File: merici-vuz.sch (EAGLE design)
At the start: 51 parts, among them IC1 MEGA328-PB, IC2 MCP73831, IC3 LE33, Q1 3,6864 MHz, Q2 IRLML6402PBF, Q4 TSM2302CX

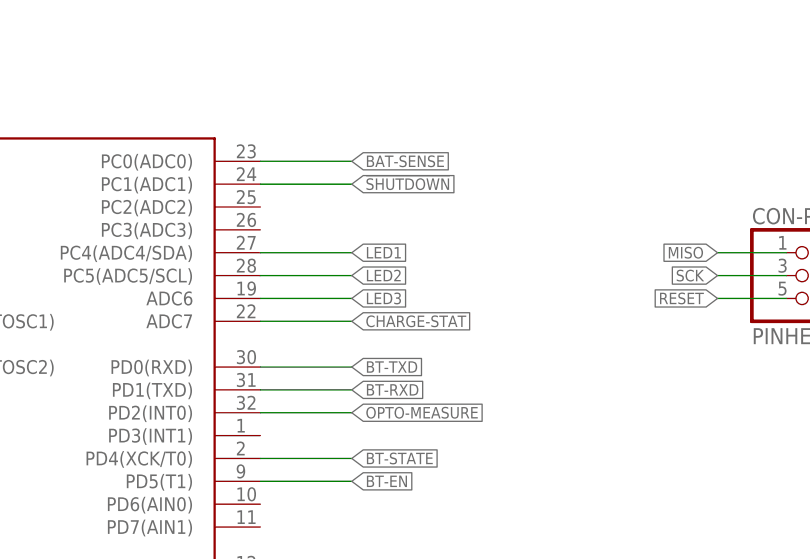
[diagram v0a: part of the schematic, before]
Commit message: Fix unconnected LEDS.
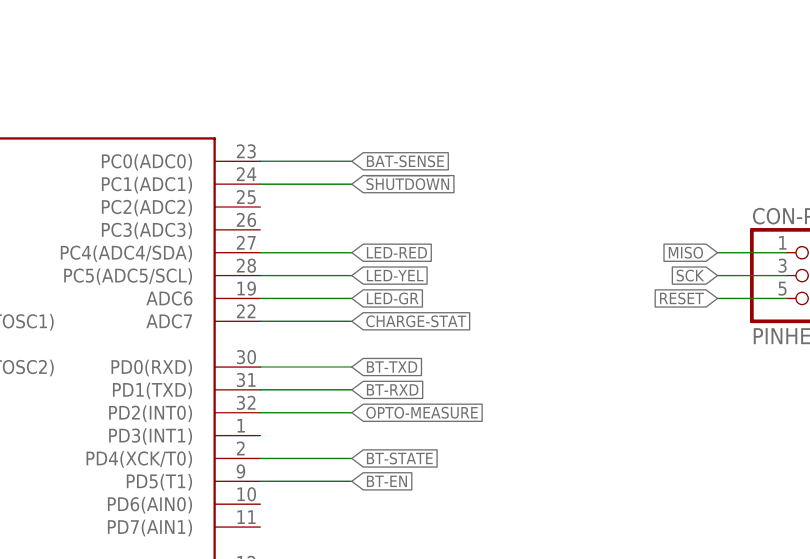
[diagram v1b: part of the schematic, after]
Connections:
- removed net LED1: IC1.PC4(ADC4/SDA)
- removed net LED2: IC1.PC5(ADC5/SCL)
- removed net LED3: IC1.ADC6
- net LED-GR: now also IC1.ADC6
- net LED-RED: now also IC1.PC4(ADC4/SDA)
- net LED-YEL: now also IC1.PC5(ADC5/SCL)
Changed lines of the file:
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@@
-</segment>
-</net>
-<net name="LED1" class="0">
-<segment>
-<pinref part="IC1" gate="G$1" pin="PC4(ADC4/SDA)"/>
-<wire x1="91.44" y1="147.32" x2="101.6" y2="147.32" width="0.1524" layer="91"/>
-<label x="101.6" y="147.32" size="1.27" layer="95" xref="yes"/>
-</segment>
-</net>
-<net name="LED2" class="0">
-<segment>
-<pinref part="IC1" gate="G$1" pin="PC5(ADC5/SCL)"/>
-<wire x1="91.44" y1="144.78" x2="101.6" y2="144.78" width="0.1524" layer="91"/>
-<label x="101.6" y="144.78" size="1.27" layer="95" xref="yes"/>
-</segment>
-</net>
-<net name="LED3" class="0">
-<segment>
-<pinref part="IC1" gate="G$1" pin="ADC6"/>
-<wire x1="91.44" y1="142.24" x2="101.6" y2="142.24" width="0.1524" layer="91"/>
-<label x="101.6" y="142.24" size="1.27" layer="95" xref="yes"/>
 </segment>
 </net>
@@
 <label x="223.52" y="129.54" size="1.27" layer="95" rot="R270" xref="yes"/>
 </segment>
+<segment>
+<pinref part="IC1" gate="G$1" pin="PC4(ADC4/SDA)"/>
+<wire x1="91.44" y1="147.32" x2="101.6" y2="147.32" width="0.1524" layer="91"/>
+<label x="101.6" y="147.32" size="1.27" layer="95" xref="yes"/>
+</segment>
 </net>
 <net name="LED-YEL" class="0">
@@
 <label x="233.68" y="129.54" size="1.27" layer="95" rot="R270" xref="yes"/>
 </segment>
+<segment>
+<pinref part="IC1" gate="G$1" pin="PC5(ADC5/SCL)"/>
+<wire x1="91.44" y1="144.78" x2="101.6" y2="144.78" width="0.1524" layer="91"/>
+<label x="101.6" y="144.78" size="1.27" layer="95" xref="yes"/>
+</segment>
 </net>
 <net name="LED-GR" class="0">
@@
 <label x="243.84" y="129.54" size="1.27" layer="95" rot="R270" xref="yes"/>
 </segment>
-</net>
+<segment>
+<pinref part="IC1" gate="G$1" pin="ADC6"/>
+<wire x1="91.44" y1="142.24" x2="101.6" y2="142.24" width="0.1524" layer="91"/>
+<label x="101.6" y="142.24" size="1.27" layer="95" xref="yes"/>
+</segment>
+</net>

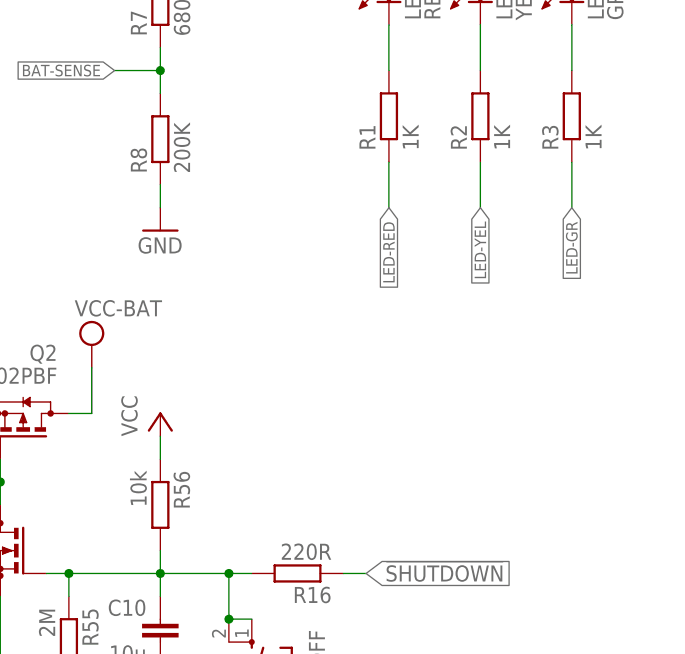
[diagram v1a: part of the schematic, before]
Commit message: Add connector for debug measuring.
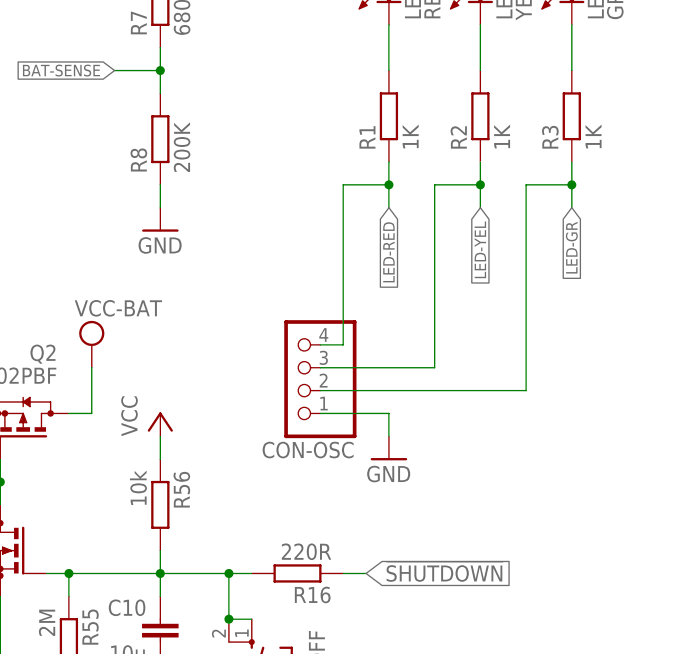
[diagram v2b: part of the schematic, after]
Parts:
- added CON-OSC: (no value), pinhead:PINHD-1X4
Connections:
- net GND: now also CON-OSC.1
- net LED-GR: now also CON-OSC.2
- net LED-RED: now also CON-OSC.4
- net LED-YEL: now also CON-OSC.3
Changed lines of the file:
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@@
 <part name="C5" library="rcl" deviceset="C-EU" device="C0805" value="10u"/>
 <part name="C6" library="rcl" deviceset="C-EU" device="C0805" value="10u"/>
+<part name="CON-OSC" library="pinhead" deviceset="PINHD-1X4" device=""/>
+<part name="GND17" library="supply1" deviceset="GND" device=""/>
 </parts>
 <sheets>
@@
 <instance part="C5" gate="G$1" x="27.94" y="63.5" rot="MR0"/>
 <instance part="C6" gate="G$1" x="180.34" y="48.26"/>
+<instance part="CON-OSC" gate="A" x="213.36" y="111.76" rot="R180"/>
+<instance part="GND17" gate="1" x="223.52" y="101.6"/>
 </instances>
 <busses>
@@
 <junction x="205.74" y="73.66"/>
 </segment>
+<segment>
+<pinref part="CON-OSC" gate="A" pin="1"/>
+<wire x1="215.9" y1="106.68" x2="223.52" y2="106.68" width="0.1524" layer="91"/>
+<pinref part="GND17" gate="1" pin="GND"/>
+<wire x1="223.52" y1="106.68" x2="223.52" y2="104.14" width="0.1524" layer="91"/>
+</segment>
 </net>
 <net name="VCC" class="0">
@@
 <net name="LED-RED" class="0">
 <segment>
+<pinref part="CON-OSC" gate="A" pin="4"/>
+<wire x1="215.9" y1="114.3" x2="218.44" y2="114.3" width="0.1524" layer="91"/>
+<wire x1="218.44" y1="114.3" x2="218.44" y2="132.08" width="0.1524" layer="91"/>
 <pinref part="R1" gate="G$1" pin="1"/>
-<wire x1="223.52" y1="134.62" x2="223.52" y2="129.54" width="0.1524" layer="91"/>
+<wire x1="223.52" y1="134.62" x2="223.52" y2="132.08" width="0.1524" layer="91"/>
 <label x="223.52" y="129.54" size="1.27" layer="95" rot="R270" xref="yes"/>
+<wire x1="223.52" y1="132.08" x2="223.52" y2="129.54" width="0.1524" layer="91"/>
+<wire x1="218.44" y1="132.08" x2="223.52" y2="132.08" width="0.1524" layer="91"/>
+<junction x="223.52" y="132.08"/>
 </segment>
 <segment>
@@
 <segment>
 <pinref part="R2" gate="G$1" pin="1"/>
-<wire x1="233.68" y1="134.62" x2="233.68" y2="129.54" width="0.1524" layer="91"/>
+<wire x1="233.68" y1="134.62" x2="233.68" y2="132.08" width="0.1524" layer="91"/>
 <label x="233.68" y="129.54" size="1.27" layer="95" rot="R270" xref="yes"/>
+<wire x1="233.68" y1="132.08" x2="233.68" y2="129.54" width="0.1524" layer="91"/>
+<junction x="233.68" y="132.08"/>
+<pinref part="CON-OSC" gate="A" pin="3"/>
+<wire x1="215.9" y1="111.76" x2="228.6" y2="111.76" width="0.1524" layer="91"/>
+<wire x1="228.6" y1="111.76" x2="228.6" y2="132.08" width="0.1524" layer="91"/>
+<wire x1="228.6" y1="132.08" x2="233.68" y2="132.08" width="0.1524" layer="91"/>
 </segment>
 <segment>
@@
 <segment>
 <pinref part="R3" gate="G$1" pin="1"/>
-<wire x1="243.84" y1="134.62" x2="243.84" y2="129.54" width="0.1524" layer="91"/>
+<wire x1="243.84" y1="134.62" x2="243.84" y2="132.08" width="0.1524" layer="91"/>
 <label x="243.84" y="129.54" size="1.27" layer="95" rot="R270" xref="yes"/>
-</segment>
-<segment>
+<wire x1="243.84" y1="132.08" x2="243.84" y2="129.54" width="0.1524" layer="91"/>
+<wire x1="238.76" y1="109.22" x2="238.76" y2="132.08" width="0.1524" layer="91"/>
+<wire x1="238.76" y1="132.08" x2="243.84" y2="132.08" width="0.1524" layer="91"/>
+<junction x="243.84" y="132.08"/>
+<pinref part="CON-OSC" gate="A" pin="2"/>
+<wire x1="215.9" y1="109.22" x2="238.76" y2="109.22" width="0.1524" layer="91"/>
+</segment>
+<segment>

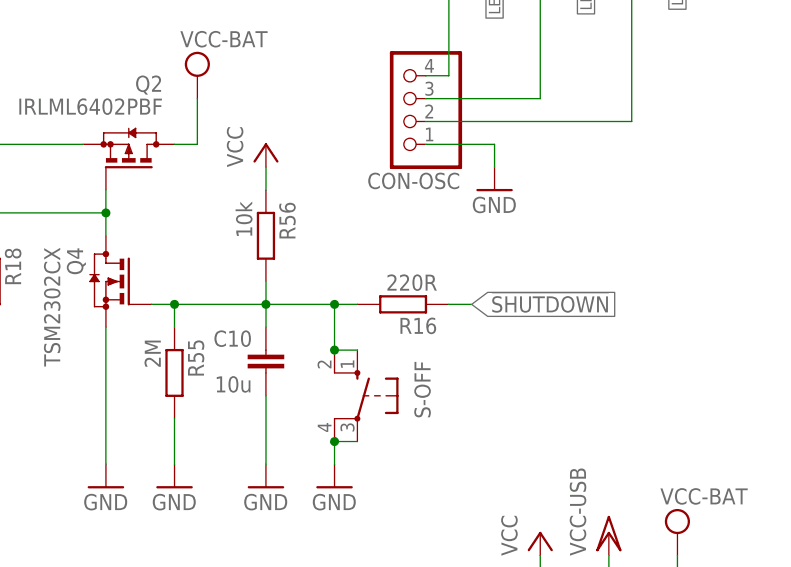
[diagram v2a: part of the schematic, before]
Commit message: Decrease current to !SHUTDOWN to 10 mA.
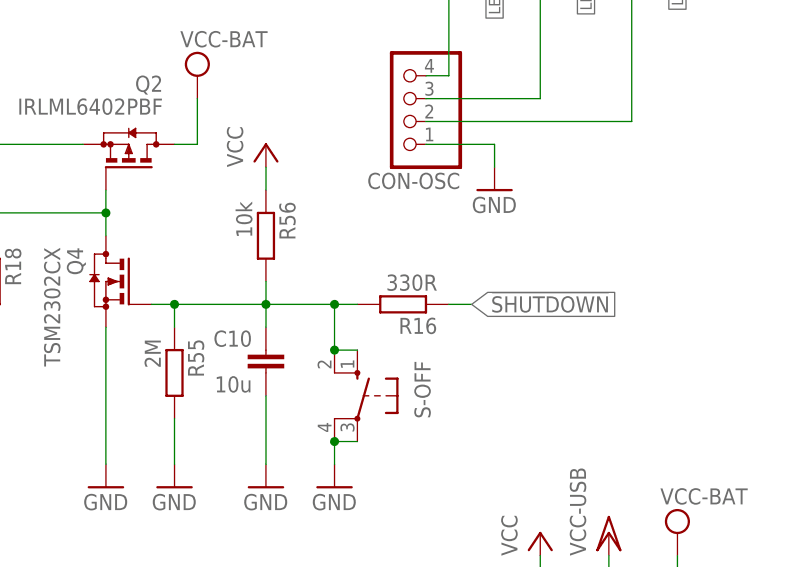
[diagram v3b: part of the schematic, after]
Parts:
- R16: value 220R -> 330R
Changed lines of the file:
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@@
 <part name="GND51" library="supply1" library_urn="urn:adsk.eagle:library:371" deviceset="GND" device=""/>
 <part name="GND52" library="supply1" library_urn="urn:adsk.eagle:library:371" deviceset="GND" device=""/>
-<part name="R16" library="rcl" deviceset="R-EU_" device="R0805" value="220R"/>
+<part name="R16" library="rcl" deviceset="R-EU_" device="R0805" value="330R"/>
 <part name="SUPPLY5" library="supply2" deviceset="VCC" device="" value="VCC-BAT"/>
 <part name="P+15" library="supply1" deviceset="VCC" device=""/>

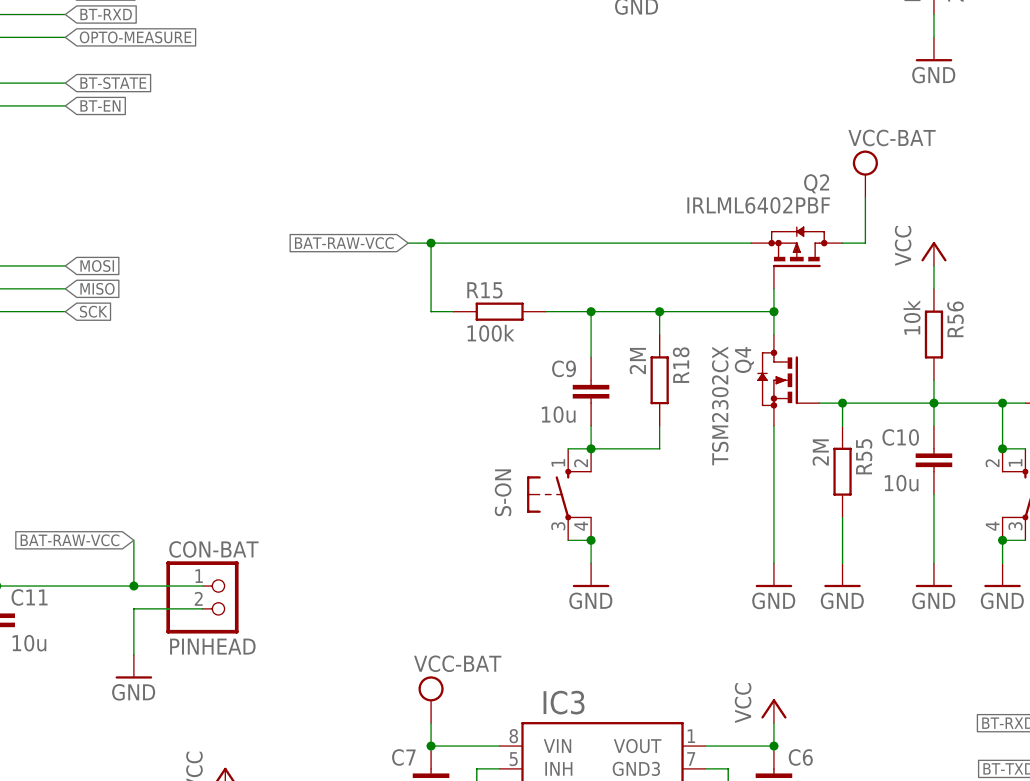
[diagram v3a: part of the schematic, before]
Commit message: Add polarity protection.
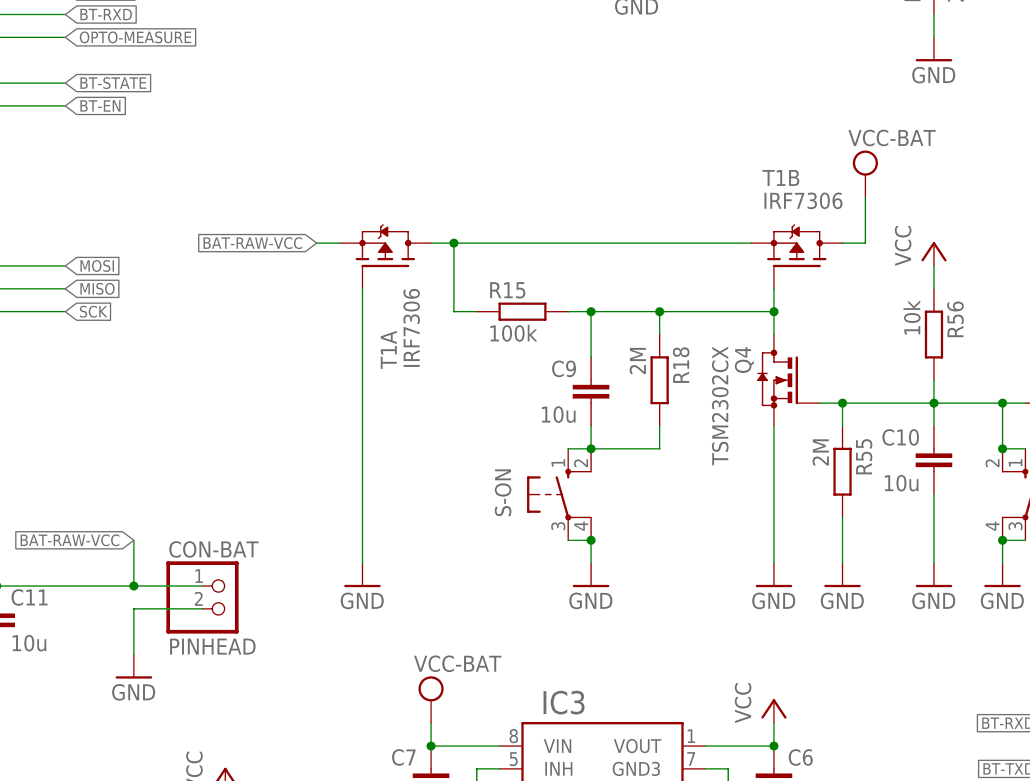
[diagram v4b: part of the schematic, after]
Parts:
- removed Q2: IRLML6402PBF, transistor-small-signal:BSS84
- added T1: IRF7306, transistor-fet:IRF7306
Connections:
- new net BAT-TRUE-VCC: R15.1, T1A.D, T1B.S
- net BAT-RAW-VCC: now also T1A.S; no longer Q2.S, R15.1
- net GND: now also T1A.G
- net START_GATE: now also T1B.G; no longer Q2.G
- net VCC: now also T1B.D; no longer Q2.D
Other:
- moved on the sheet: R15
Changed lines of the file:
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@@
 <part name="LED4" library="led" deviceset="LED" device="CHIP-LED0805"/>
 <part name="R14" library="rcl" deviceset="R-EU_" device="R0805" value="1K"/>
-<part name="Q2" library="transistor-small-signal" deviceset="BSS84" device="" value="IRLML6402PBF"/>
 <part name="C9" library="rcl" deviceset="C-EU" device="C0805" value="10u"/>
 <part name="R55" library="rcl" deviceset="R-EU_" device="R0805" value="2M"/>
@@
 <part name="CON-OSC" library="pinhead" deviceset="PINHD-1X4" device=""/>
 <part name="GND17" library="supply1" deviceset="GND" device=""/>
+<part name="T1" library="transistor-fet" deviceset="IRF7306" device=""/>
+<part name="GND18" library="supply1" library_urn="urn:adsk.eagle:library:371" deviceset="GND" device=""/>
 </parts>
 <sheets>
@@
 <instance part="LED4" gate="G$1" x="35.56" y="78.74" rot="R90"/>
 <instance part="R14" gate="G$1" x="48.26" y="73.66" rot="R90"/>
-<instance part="Q2" gate="G$1" x="182.88" y="106.68" smashed="yes" rot="R90">
-<attribute name="VALUE" x="186.69" y="111.76" size="1.778" layer="96" rot="R180"/>
-<attribute name="NAME" x="186.69" y="114.3" size="1.778" layer="95" rot="R180"/>
-</instance>
 <instance part="C9" gate="G$1" x="160.02" y="91.44" rot="MR0"/>
 <instance part="R55" gate="G$1" x="187.96" y="81.28" rot="R270"/>
 <instance part="R56" gate="G$1" x="198.12" y="96.52" rot="R270"/>
 <instance part="C10" gate="G$1" x="198.12" y="83.82" rot="MR0"/>
-<instance part="R15" gate="G$1" x="149.86" y="99.06"/>
+<instance part="R15" gate="G$1" x="152.4" y="99.06"/>
 <instance part="Q4" gate="G$1" x="180.34" y="91.44" smashed="yes" rot="MR0">
 <attribute name="VALUE" x="175.26" y="95.25" size="1.778" layer="96" rot="MR270"/>
@@
 <instance part="CON-OSC" gate="A" x="213.36" y="111.76" rot="R180"/>
 <instance part="GND17" gate="1" x="223.52" y="101.6"/>
+<instance part="T1" gate="A" x="137.16" y="104.14" rot="R90"/>
+<instance part="T1" gate="B" x="182.88" y="104.14" smashed="yes" rot="R90">
+<attribute name="VALUE" x="179.07" y="110.49" size="1.778" layer="96"/>
+<attribute name="NAME" x="179.07" y="113.03" size="1.778" layer="95"/>
+</instance>
+<instance part="GND18" gate="1" x="134.62" y="68.58"/>
 </instances>
 <busses>
@@
 <wire x1="223.52" y1="106.68" x2="223.52" y2="104.14" width="0.1524" layer="91"/>
 </segment>
+<segment>
+<pinref part="GND18" gate="1" pin="GND"/>
+<pinref part="T1" gate="A" pin="G"/>
+<wire x1="134.62" y1="71.12" x2="134.62" y2="101.6" width="0.1524" layer="91"/>
+</segment>
 </net>
 <net name="VCC" class="0">
@@
 </segment>
 <segment>
-<pinref part="Q2" gate="G$1" pin="D"/>
 <wire x1="187.96" y1="106.68" x2="190.5" y2="106.68" width="0.1524" layer="91"/>
 <pinref part="SUPPLY5" gate="G$1" pin="VCC"/>
 <wire x1="190.5" y1="106.68" x2="190.5" y2="111.76" width="0.1524" layer="91"/>
+<pinref part="T1" gate="B" pin="D"/>
 </segment>
 <segment>
@@
 <segment>
 <pinref part="R15" gate="G$1" pin="2"/>
-<wire x1="154.94" y1="99.06" x2="160.02" y2="99.06" width="0.1524" layer="91"/>
+<wire x1="157.48" y1="99.06" x2="160.02" y2="99.06" width="0.1524" layer="91"/>
 <wire x1="160.02" y1="99.06" x2="167.64" y2="99.06" width="0.1524" layer="91"/>
 <pinref part="C9" gate="G$1" pin="1"/>
@@
 <pinref part="R18" gate="G$1" pin="1"/>
 <wire x1="167.64" y1="96.52" x2="167.64" y2="99.06" width="0.1524" layer="91"/>
-<pinref part="Q2" gate="G$1" pin="G"/>
 <pinref part="Q4" gate="G$1" pin="D"/>
 <wire x1="180.34" y1="96.52" x2="180.34" y2="99.06" width="0.1524" layer="91"/>
@@
 <junction x="167.64" y="99.06"/>
 <junction x="180.34" y="99.06"/>
+<pinref part="T1" gate="B" pin="G"/>
 </segment>
 </net>
@@
 </net>
 <net name="BAT-RAW-VCC" class="0">
-<segment>
-<pinref part="Q2" gate="G$1" pin="S"/>
-<pinref part="R15" gate="G$1" pin="1"/>
-<wire x1="144.78" y1="99.06" x2="142.24" y2="99.06" width="0.1524" layer="91"/>
-<wire x1="142.24" y1="99.06" x2="142.24" y2="106.68" width="0.1524" layer="91"/>
-<wire x1="142.24" y1="106.68" x2="177.8" y2="106.68" width="0.1524" layer="91"/>
-<wire x1="139.7" y1="106.68" x2="142.24" y2="106.68" width="0.1524" layer="91"/>
-<junction x="142.24" y="106.68"/>
-<label x="139.7" y="106.68" size="1.27" layer="95" rot="R180" xref="yes"/>
-</segment>
 <segment>
 <pinref part="CON-BAT" gate="G$1" pin="1"/>
@@
 <junction x="93.98" y="68.58"/>
 </segment>
+<segment>
+<pinref part="T1" gate="A" pin="S"/>
+<wire x1="129.54" y1="106.68" x2="132.08" y2="106.68" width="0.1524" layer="91"/>
+<label x="129.54" y="106.68" size="1.27" layer="95" rot="R180" xref="yes"/>
+</segment>
 </net>
 <net name="LED-RED" class="0">
@@
 </segment>
 </net>
+<net name="BAT-TRUE-VCC" class="0">
+<segment>
+<pinref part="R15" gate="G$1" pin="1"/>
+<wire x1="147.32" y1="99.06" x2="144.78" y2="99.06" width="0.1524" layer="91"/>
+<wire x1="144.78" y1="99.06" x2="144.78" y2="106.68" width="0.1524" layer="91"/>
+<wire x1="144.78" y1="106.68" x2="177.8" y2="106.68" width="0.1524" layer="91"/>
+<junction x="144.78" y="106.68"/>
+<pinref part="T1" gate="B" pin="S"/>
+<pinref part="T1" gate="A" pin="D"/>
+<wire x1="142.24" y1="106.68" x2="144.78" y2="106.68" width="0.1524" layer="91"/>
+</segment>
+</net>
